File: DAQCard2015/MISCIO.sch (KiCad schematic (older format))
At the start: 34 parts, among them K1 1462042-8, P10 SPYPAD, P11 70246-1004, P3 miniDIL20, P4 LEMO_EPY.00.250.NTN, P5 LEMO_EPY.00.250.NTN, P6 FAN, P8 SPYPAD, P9 SHV, Q1 MMBT2222A-TP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

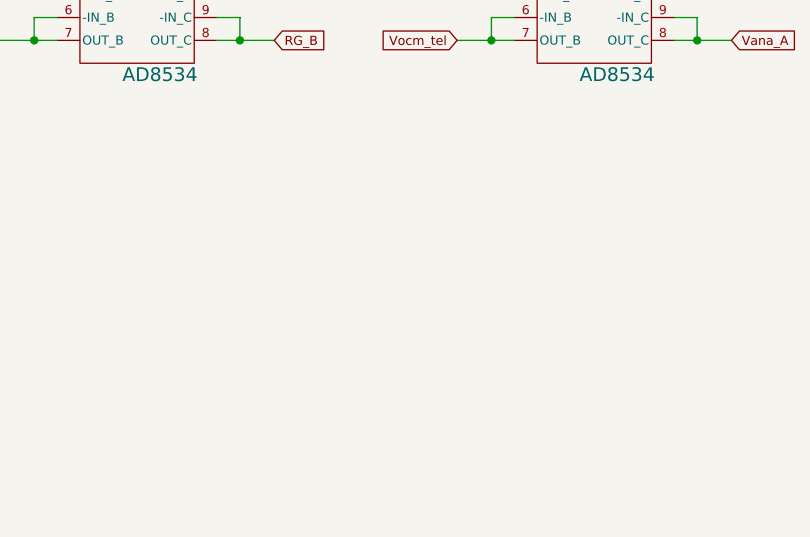
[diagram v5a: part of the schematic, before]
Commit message: Update V1.0 of DAQ Board Includes LED Driver for RJ45 Port, repositioning of JTAG
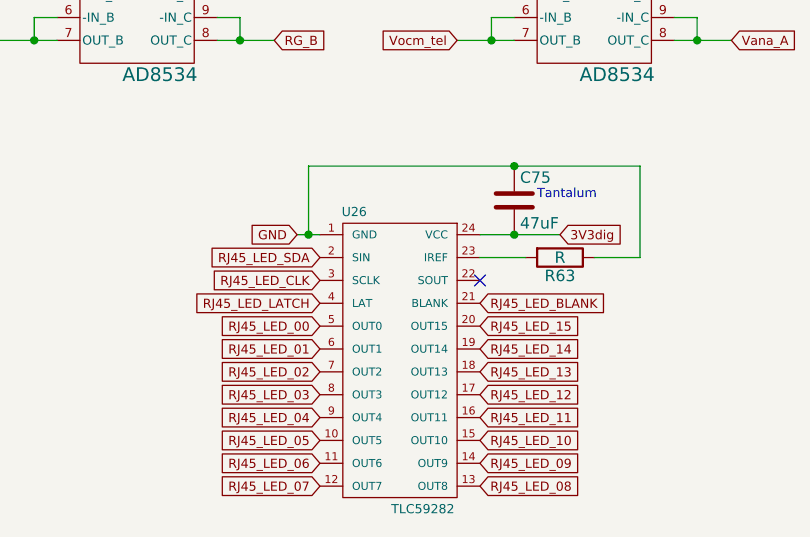
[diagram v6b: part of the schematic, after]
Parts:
- added C75: 47uF, Capacitors_Tantalum_SMD:TantalC_SizeD_EIA-7343_Reflow, symbol C
- added R63: R, Resistors_SMD:R_0603_HandSoldering, symbol R
- added U26: TLC59282, Housings_SSOP:SSOP-24_3.9x8.7mm_Pitch0.635mm, symbol TLC59282
- P10, P8: value SPYPAD -> GND
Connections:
- net 3V3dig: now also C75.2, U26.24 (VCC)
- net GND: now also C75.1, R63.1, U26.1 (GND)
- new net: R63.2, U26.23 (IREF)
- new net RJ45_LED_00: U26.5 (OUT0)
- new net RJ45_LED_01: U26.6 (OUT1)
- new net RJ45_LED_02: U26.7 (OUT2)
- new net RJ45_LED_03: U26.8 (OUT3)
- new net RJ45_LED_04: U26.9 (OUT4)
- new net RJ45_LED_05: U26.10 (OUT5)
- new net RJ45_LED_06: U26.11 (OUT6)
- new net RJ45_LED_07: U26.12 (OUT7)
- new net RJ45_LED_08: U26.13 (OUT8)
- new net RJ45_LED_09: U26.14 (OUT9)
- new net RJ45_LED_10: U26.15 (OUT10)
- new net RJ45_LED_11: U26.16 (OUT11)
- new net RJ45_LED_12: U26.17 (OUT12)
- new net RJ45_LED_13: U26.18 (OUT13)
- new net RJ45_LED_14: U26.19 (OUT14)
- new net RJ45_LED_15: U26.20 (OUT15)
- new net RJ45_LED_BLANK: U26.21 (BLANK)
- new net RJ45_LED_CLK: U26.3 (SCLK)
- new net RJ45_LED_LATCH: U26.4 (LAT)
- new net RJ45_LED_SDA: U26.2 (SIN)
- no-connect marks 4 -> 5
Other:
- note added: "Tantalum"
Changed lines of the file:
@@
 P 8250 5750
 F 0 "P8" H 8330 5750 40  0000 L CNN
-F 1 "SPYPAD" H 8250 5800 30  0001 C CNN
+F 1 "GND" H 8250 5800 30  0001 C CNN
 F 2 "extras:Harwin_D3082-05" H 8250 5750 60  0001 C CNN
 F 3 "" H 8250 5750 60  0000 C CNN
@@
 P 8400 5750
 F 0 "P10" H 8480 5750 40  0000 L CNN
-F 1 "SPYPAD" H 8400 5800 30  0001 C CNN
+F 1 "GND" H 8400 5800 30  0001 C CNN
 F 2 "extras:Harwin_D3082-05" H 8400 5750 60  0001 C CNN
 F 3 "" H 8400 5750 60  0000 C CNN
@@
 Wire Wire Line
 	1700 3350 2400 3350
+$Comp
+L TLC59282 U26
+U 1 1 560DFA19
+P 3100 6700
+F 0 "U26" H 2900 7350 40  0000 C CNN
+F 1 "TLC59282" H 3200 6050 40  0000 C CNN
+F 2 "Housings_SSOP:SSOP-24_3.9x8.7mm_Pitch0.635mm" H 3100 6700 40  0001 C CNN
+F 3 "" H 3100 6700 40  0000 C CNN
+	1    3100 6700
+	1    0    0    -1
+$EndComp
+Text GLabel 2650 6150 0    40   Input ~ 0
+GND
+Text GLabel 3800 6150 2    40   Input ~ 0
+3V3dig
+Wire Wire Line
+	3450 6150 3800 6150
+$Comp
+L C C75
+U 1 1 560DFC66
+P 3600 6000
+F 0 "C75" H 3625 6100 50  0000 L CNN
+F 1 "47uF" H 3625 5900 50  0000 L CNN
+F 2 "Capacitors_Tantalum_SMD:TantalC_SizeD_EIA-7343_Reflow" H 3638 5850 30  0001 C CNN
+F 3 "" H 3600 6000 60  0000 C CNN
+	1    3600 6000
+	1    0    0    -1
+$EndComp
+Connection ~ 3600 6150
+Wire Wire Line
+	2700 5850 4150 5850
+Wire Wire Line
+	2750 6150 2650 6150
+Wire Wire Line
+	2700 5850 2700 6150
+Connection ~ 2700 6150
+Text Notes 3700 6000 0    40   ~ 0
+Tantalum
+Text GLabel 2750 6250 0    40   Input ~ 0
+RJ45_LED_SDA
+Text GLabel 2750 6350 0    40   Input ~ 0
+RJ45_LED_CLK
+Text GLabel 2750 6450 0    40   Input ~ 0
+RJ45_LED_LATCH
+Text GLabel 3450 6450 2    40   Input ~ 0
+RJ45_LED_BLANK
+NoConn ~ 3450 6350
+$Comp
+L R R63
+U 1 1 560E0E6E
+P 3800 6250
+F 0 "R63" V 3880 6250 50  0000 C CNN
+F 1 "R" V 3800 6250 50  0000 C CNN
+F 2 "Resistors_SMD:R_0603_HandSoldering" V 3730 6250 30  0001 C CNN
+F 3 "" H 3800 6250 30  0000 C CNN
+	1    3800 6250
+	0    1    1    0
+$EndComp
+Wire Wire Line
+	3650 6250 3450 6250
+Wire Wire Line
+	3950 6250 4150 6250
+Wire Wire Line
+	4150 6250 4150 5850
+Connection ~ 3600 5850
+Text GLabel 2750 6550 0    40   Input ~ 0
+RJ45_LED_00
+Text GLabel 2750 6650 0    40   Input ~ 0
+RJ45_LED_01
+Text GLabel 2750 6750 0    40   Input ~ 0
+RJ45_LED_02
+Text GLabel 2750 6850 0    40   Input ~ 0
+RJ45_LED_03
+Text GLabel 2750 6950 0    40   Input ~ 0
+RJ45_LED_04
+Text GLabel 2750 7050 0    40   Input ~ 0
+RJ45_LED_05
+Text GLabel 2750 7150 0    40   Input ~ 0
+RJ45_LED_06
+Text GLabel 2750 7250 0    40   Input ~ 0
+RJ45_LED_07
+Text GLabel 3450 7250 2    40   Input ~ 0
+RJ45_LED_08
+Text GLabel 3450 7150 2    40   Input ~ 0
+RJ45_LED_09
+Text GLabel 3450 7050 2    40   Input ~ 0
+RJ45_LED_10
+Text GLabel 3450 6950 2    40   Input ~ 0
+RJ45_LED_11
+Text GLabel 3450 6850 2    40   Input ~ 0
+RJ45_LED_12
+Text GLabel 3450 6650 2    40   Input ~ 0
+RJ45_LED_14
+Text GLabel 3450 6750 2    40   Input ~ 0
+RJ45_LED_13
+Text GLabel 3450 6550 2    40   Input ~ 0
+RJ45_LED_15
 $EndSCHEMATC

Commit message: Adds digipart field to all parts that is now used in automatic generation of BOM(see DAQCard2015.html)
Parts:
- added C77, C79: 10uF, Capacitors_SMD:C_0805, symbol C
- added P18: Aref_A, extras:testpad, symbol SPYPAD
- added P19: Aref_B, extras:testpad, symbol SPYPAD
- added P20: RG_A, extras:testpad, symbol SPYPAD
- added P21: RG_B, extras:testpad, symbol SPYPAD
- added P22: Vthresh, extras:testpad, symbol SPYPAD
- added P23: Vocm, extras:testpad, symbol SPYPAD
- added P24: Vana_B, extras:testpad, symbol SPYPAD
- added P25: Vana_A, extras:testpad, symbol SPYPAD
- added P26: CASE GND, extras:TE_1217133-1, symbol SHV
- C70: digipart (none) -> 478-2991-1-ND
- C75: digipart (none) -> 478-9200-1-ND
- C76: digipart (none) -> 445-1316-1-ND
- D1: digipart (none) -> 350-3555-ND
- D2: digipart (none) -> SMAJ75ALFCT-ND
- K1: digipart (none) -> PB1249CT-ND
- P11: digipart (none) -> WM3478-ND
- P3: digipart (none) -> 952-1392-ND
- P4, P5: digipart (none) -> 1124-1358-ND
- P6: digipart (none) -> A1921-ND
- P9: value SHV -> HV; digipart (none) -> A100449CT-ND
- Q1, Q2: digipart (none) -> MMBT2222ATPMSCT-ND
- R50: value R -> 300R; digipart (none) -> P300HCT-ND
- R51, R52, R62: value R -> 30R; digipart (none) -> P30.0HCT-ND
- R53, R54: digipart (none) -> P10.0KHCT-ND
- R55: digipart (none) -> P49.9KFCT-ND
- R56: value 253R -> 249R; digipart (none) -> P249HCT-ND
- R57, R59: digipart (none) -> P470KECT-ND
- R58, R60: digipart (none) -> P51KECT-ND
- R61: digipart (none) -> P5.10KHCT-ND
- R63: value R -> 2k; digipart (none) -> P2.00KHCT-ND
- RV1: digipart (none) -> SM-31TW103CT-ND
- TH1: digipart (none) -> 445-2554-1-ND
- U19, U23: digipart (none) -> AD8534ARUZ-REELCT-ND
- U22: digipart (none) -> AD5628ARUZ-2-ND
- U24: digipart (none) -> MCP65R41T-2402E/CHYCT-ND
- U26: digipart (none) -> 296-28098-1-ND
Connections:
- net 5Vdig: now also C77.2, C79.2
- net Aref_A: now also P18.1
- net Aref_B: now also P19.1
- net GND: now also C77.1, C79.1, P26.1 (In)
- net RG_A: now also P20.1
- net RG_B: now also P21.1
- net Vana_A: now also P25.1
- net Vana_B: now also P24.1
- net Vocm_tel: now also P23.1
- net Vthresh: now also P22.1
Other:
- moved on the sheet: U23

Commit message: annotates parts for new build-management tool
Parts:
- C70: Digikey (none) -> 478-2991-1-ND; digipart 478-2991-1-ND -> (none)
- C75: Digikey (none) -> 478-9200-1-ND; digipart 478-9200-1-ND -> (none)
- C76: Digikey (none) -> 445-1316-1-ND; digipart 445-1316-1-ND -> (none)
- C77, C79: Digikey (none) -> 445-11464-1-ND; digipart 445-11464-1-ND -> (none)
- D1: Digikey (none) -> 350-3555-ND; digipart 350-3555-ND -> (none)
- D2: Digikey (none) -> SMAJ75ALFCT-ND; digipart SMAJ75ALFCT-ND -> (none)
- K1: Digikey (none) -> PB1249CT-ND; digipart PB1249CT-ND -> (none)
- P11: Digikey (none) -> WM3478-ND; digipart WM3478-ND -> (none)
- P26, P9: Digikey (none) -> A100449CT-ND; digipart A100449CT-ND -> (none)
- P3: Digikey (none) -> 952-1392-ND; digipart 952-1392-ND -> (none)
- P4, P5: Digikey (none) -> 1124-1358-ND; digipart 1124-1358-ND -> (none)
- P6: Digikey (none) -> A1921-ND; digipart A1921-ND -> (none)
- Q1, Q2: Digikey (none) -> MMBT2222ATPMSCT-ND; digipart MMBT2222ATPMSCT-ND -> (none)
- R50: Digikey (none) -> P300HCT-ND; digipart P300HCT-ND -> (none)
- R51, R52, R62: Digikey (none) -> P30.0HCT-ND; digipart P30.0HCT-ND -> (none)
- R53, R54: Digikey (none) -> P10.0KHCT-ND; digipart P10.0KHCT-ND -> (none)
- R55: Digikey (none) -> P49.9KFCT-ND; digipart P49.9KFCT-ND -> (none)
- R56: Digikey (none) -> P249HCT-ND; digipart P249HCT-ND -> (none)
- R57, R59: Digikey (none) -> P470KECT-ND; digipart P470KECT-ND -> (none)
- R58, R60: Digikey (none) -> P51KECT-ND; digipart P51KECT-ND -> (none)
- R61: Digikey (none) -> P5.10KHCT-ND; digipart P5.10KHCT-ND -> (none)
- R63: Digikey (none) -> P2.00KHCT-ND; digipart P2.00KHCT-ND -> (none)
- RV1: symbol POT -> POT-RESCUE-DAQCard2015; Digikey (none) -> SM-31TW103CT-ND; digipart SM-31TW103CT-ND -> (none)
- TH1: Digikey (none) -> 445-2554-1-ND; digipart 445-2554-1-ND -> (none)
- U19, U23: Digikey (none) -> AD8534ARUZ-REELCT-ND; digipart AD8534ARUZ-REELCT-ND -> (none)
- U22: Digikey (none) -> AD5628ARUZ-2-ND; digipart AD5628ARUZ-2-ND -> (none)
- U24: Digikey (none) -> MCP65R41T-2402E/CHYCT-ND; digipart MCP65R41T-2402E/CHYCT-ND -> (none)
- U26: Digikey (none) -> 296-28098-1-ND; digipart 296-28098-1-ND -> (none)
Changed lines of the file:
@@
 EESchema Schematic File Version 2
+LIBS:DAQCard2015-rescue
 LIBS:power
 LIBS:device
@@
 F 2 "extras:EPY.00.250.NTN" H 10650 1350 60  0001 C CNN
 F 3 "" H 10650 1350 60  0000 C CNN
-F 4 "1124-1358-ND" H 10650 1350 60  0001 C CNN "digipart"
+F 4 "1124-1358-ND" H 10650 1350 60  0001 C CNN "Digikey"
 	1    10650 1350
 	1    0    0    -1
@@
 F 2 "extras:EPY.00.250.NTN" H 10400 1950 60  0001 C CNN
 F 3 "" H 10400 1950 60  0000 C CNN
-F 4 "1124-1358-ND" H 10400 1950 60  0001 C CNN "digipart"
+F 4 "1124-1358-ND" H 10400 1950 60  0001 C CNN "Digikey"
 	1    10400 1950
 	1    0    0    -1
@@
 F 2 "extras:M50-3101045" H 9250 1800 60  0001 C CNN
 F 3 "" H 9250 1800 60  0000 C CNN
-F 4 "952-1392-ND" H 9250 1800 60  0001 C CNN "digipart"
+F 4 "952-1392-ND" H 9250 1800 60  0001 C CNN "Digikey"
 	1    9250 1800
 	1    0    0    -1
@@
 F 2 "Resistors_SMD:R_0603" V 8030 3750 30  0001 C CNN
 F 3 "" H 8100 3750 30  0000 C CNN
-F 4 "P10.0KHCT-ND" V 8100 3750 60  0001 C CNN "digipart"
+F 4 "P10.0KHCT-ND" V 8100 3750 60  0001 C CNN "Digikey"
 	1    8100 3750
 	1    0    0    -1
@@
 F 2 "Resistors_SMD:R_0603" V 8530 3750 30  0001 C CNN
 F 3 "" H 8600 3750 30  0000 C CNN
-F 4 "P10.0KHCT-ND" V 8600 3750 60  0001 C CNN "digipart"
+F 4 "P10.0KHCT-ND" V 8600 3750 60  0001 C CNN "Digikey"
 	1    8600 3750
 	1    0    0    -1
 $EndComp
 $Comp
-L POT RV1
+L POT-RESCUE-DAQCard2015 RV1
 U 1 1 55F0172C
 P 8100 4550
+AR Path="/55F0172C" Ref="RV1"  Part="1"
+AR Path="/55C9D43F/55F0172C" Ref="RV1"  Part="1"
 F 0 "RV1" H 8100 4450 50  0000 C CNN
 F 1 "10k" H 8100 4550 50  0000 C CNN
 F 2 "extras:SM31TW+0805" H 8100 4550 60  0001 C CNN
 F 3 "" H 8100 4550 60  0000 C CNN
-F 4 "SM-31TW103CT-ND" H 8100 4550 60  0001 C CNN "digipart"
+F 4 "SM-31TW103CT-ND" H 8100 4550 60  0001 C CNN "Digikey"
 	1    8100 4550
 	0    1    1    0
@@
 F 2 "Housings_SOT-23_SOT-143_TSOT-6:SOT-23-6" H 9100 4050 60  0001 C CNN
 F 3 "" H 9100 4050 60  0000 C CNN
-F 4 "MCP65R41T-2402E/CHYCT-ND" H 9100 4050 60  0001 C CNN "digipart"
+F 4 "MCP65R41T-2402E/CHYCT-ND" H 9100 4050 60  0001 C CNN "Digikey"
 	1    9100 4050
 	1    0    0    -1
@@
 F 2 "Resistors_SMD:R_0603" H 8600 4450 60  0001 C CNN
 F 3 "" H 8600 4450 60  0000 C CNN
-F 4 "445-2554-1-ND" V 8600 4450 60  0001 C CNN "digipart"
+F 4 "445-2554-1-ND" V 8600 4450 60  0001 C CNN "Digikey"
 	1    8600 4450
 	1    0    0    -1
@@
 F 2 "Resistors_SMD:R_0603" V 9680 4050 30  0001 C CNN
 F 3 "" H 9750 4050 30  0000 C CNN
-F 4 "P249HCT-ND" V 9750 4050 60  0001 C CNN "digipart"
+F 4 "P249HCT-ND" V 9750 4050 60  0001 C CNN "Digikey"
 	1    9750 4050
 	0    1    1    0
@@
 F 2 "Socket_Strips:Socket_Strip_Straight_1x02" H 10500 3650 60  0001 C CNN
 F 3 "" H 10500 3650 60  0000 C CNN
-F 4 "A1921-ND" H 10500 3650 60  0001 C CNN "digipart"
+F 4 "A1921-ND" H 10500 3650 60  0001 C CNN "Digikey"
 	1    10500 3650
 	1    0    0    -1
@@
 F 2 "Resistors_SMD:R_1206" V 8980 4350 30  0001 C CNN
 F 3 "" H 9050 4350 30  0000 C CNN
-F 4 "P49.9KFCT-ND" V 9050 4350 60  0001 C CNN "digipart"
+F 4 "P49.9KFCT-ND" V 9050 4350 60  0001 C CNN "Digikey"
 	1    9050 4350
 	0    1    1    0
@@
 F 2 "extras:1462042-8" H 3250 1050 60  0001 C CNN
 F 3 "" H 3250 1050 60  0000 C CNN
-F 4 "PB1249CT-ND" H 3250 1050 60  0001 C CNN "digipart"
+F 4 "PB1249CT-ND" H 3250 1050 60  0001 C CNN "Digikey"
 	1    3250 1050
 	1    0    0    -1
@@
 F 2 "Resistors_SMD:R_1206" V 2530 900 30  0001 C CNN
 F 3 "" H 2600 900 30  0000 C CNN
-F 4 "P470KECT-ND" V 2600 900 60  0001 C CNN "digipart"
+F 4 "P470KECT-ND" V 2600 900 60  0001 C CNN "Digikey"
 	1    2600 900
 	0    1    1    0
@@
 F 2 "Resistors_SMD:R_1206" V 2230 1250 30  0001 C CNN
 F 3 "" H 2300 1250 30  0000 C CNN
-F 4 "P470KECT-ND" V 2300 1250 60  0001 C CNN "digipart"
+F 4 "P470KECT-ND" V 2300 1250 60  0001 C CNN "Digikey"
 	1    2300 1250
 	0    1    1    0
@@
 F 2 "Capacitors_SMD:C_1812" H 1688 1300 30  0001 C CNN
 F 3 "" H 1650 1450 60  0000 C CNN
-F 4 "478-2991-1-ND" H 1650 1450 60  0001 C CNN "digipart"
+F 4 "478-2991-1-ND" H 1650 1450 60  0001 C CNN "Digikey"
 	1    1650 1450
 	1    0    0    -1
@@
 F 2 "Resistors_SMD:R_1206" V 2680 1650 30  0001 C CNN
 F 3 "" H 2750 1650 30  0000 C CNN
-F 4 "P51KECT-ND" V 2750 1650 60  0001 C CNN "digipart"
+F 4 "P51KECT-ND" V 2750 1650 60  0001 C CNN "Digikey"
 	1    2750 1650
 	0    1    1    0
@@
 F 2 "Resistors_SMD:R_1206" V 2280 1650 30  0001 C CNN
 F 3 "" H 2350 1650 30  0000 C CNN
-F 4 "P51KECT-ND" V 2350 1650 60  0001 C CNN "digipart"
+F 4 "P51KECT-ND" V 2350 1650 60  0001 C CNN "Digikey"
 	1    2350 1650
 	0    1    1    0
@@
 F 2 "Diodes_SMD:SMA_Standard" V 4000 1350 60  0001 C CNN
 F 3 "" V 4000 1350 60  0000 C CNN
-F 4 "SMAJ75ALFCT-ND" H 4000 1350 60  0001 C CNN "digipart"
+F 4 "SMAJ75ALFCT-ND" H 4000 1350 60  0001 C CNN "Digikey"
 	1    4000 1350
 	0    1    1    0
@@
 F 2 "Resistors_SMD:R_0603" V 4430 1800 30  0001 C CNN
 F 3 "" H 4500 1800 30  0000 C CNN
-F 4 "P5.10KHCT-ND" V 4500 1800 60  0001 C CNN "digipart"
+F 4 "P5.10KHCT-ND" V 4500 1800 60  0001 C CNN "Digikey"
 	1    4500 1800
 	0    1    1    0
@@
 F 2 "extras:TE_1217133-1" H 1850 1000 60  0001 C CNN
 F 3 "" H 1850 1000 60  0000 C CNN
-F 4 "A100449CT-ND" H 1850 1000 60  0001 C CNN "digipart"
+F 4 "A100449CT-ND" H 1850 1000 60  0001 C CNN "Digikey"
 	1    1850 1000
 	-1   0    0    1
@@
 F 2 "extras:Dialight_5690101372F" H 6350 1800 60  0001 C CNN
 F 3 "" H 6350 1800 60  0000 C CNN
-F 4 "350-3555-ND" V 6350 1800 60  0001 C CNN "digipart"
+F 4 "350-3555-ND" V 6350 1800 60  0001 C CNN "Digikey"
 	1    6350 1800
 	1    0    0    -1
@@
 F 2 "Resistors_SMD:R_0603" V 6280 1300 30  0001 C CNN
 F 3 "" H 6350 1300 30  0000 C CNN
-F 4 "P300HCT-ND" V 6350 1300 60  0001 C CNN "digipart"
+F 4 "P300HCT-ND" V 6350 1300 60  0001 C CNN "Digikey"
 	1    6350 1300
 	1    0    0    -1
@@
 F 2 "Resistors_SMD:R_0603" V 6580 1300 30  0001 C CNN
 F 3 "" H 6650 1300 30  0000 C CNN
-F 4 "P30.0HCT-ND" V 6650 1300 60  0001 C CNN "digipart"
+F 4 "P30.0HCT-ND" V 6650 1300 60  0001 C CNN "Digikey"
 	1    6650 1300
 	1    0    0    -1
@@
 F 2 "Resistors_SMD:R_0603" V 6880 1300 30  0001 C CNN
 F 3 "" H 6950 1300 30  0000 C CNN
-F 4 "P30.0HCT-ND" V 6950 1300 60  0001 C CNN "digipart"
+F 4 "P30.0HCT-ND" V 6950 1300 60  0001 C CNN "Digikey"
 	1    6950 1300
 	1    0    0    -1
@@
 F 2 "Resistors_SMD:R_0603" V 7180 1300 30  0001 C CNN
 F 3 "" H 7250 1300 30  0000 C CNN
-F 4 "P30.0HCT-ND" V 7250 1300 60  0001 C CNN "digipart"
+F 4 "P30.0HCT-ND" V 7250 1300 60  0001 C CNN "Digikey"
 	1    7250 1300
 	1    0    0    -1
@@
 F 2 "Housings_SOT-23_SOT-143_TSOT-6:SOT-23" H 10400 4150 29  0001 C CNN
 F 3 "" H 10200 4050 60  0000 C CNN
-F 4 "MMBT2222ATPMSCT-ND" H 10200 4050 60  0001 C CNN "digipart"
+F 4 "MMBT2222ATPMSCT-ND" H 10200 4050 60  0001 C CNN "Digikey"
 	1    10200 4050
 	1    0    0    -1
@@
 F 2 "extras:TSSOP-16_4.4x5mm_Pitch0.65mm" H 3150 3650 60  0001 C CNN
 F 3 "" H 3150 3650 60  0000 C CNN
-F 4 "AD5628ARUZ-2-ND" H 2950 3500 60  0001 C CNN "digipart"
+F 4 "AD5628ARUZ-2-ND" H 2950 3500 60  0001 C CNN "Digikey"
 	1    2950 3500
 	1    0    0    -1
@@
 F 2 "Housings_SSOP:TSSOP-14_4.4x5mm_Pitch0.65mm" H 1850 5150 60  0001 C CNN
 F 3 "" H 1850 5150 60  0000 C CNN
-F 4 "AD8534ARUZ-REELCT-ND" H 1950 5000 60  0001 C CNN "digipart"
+F 4 "AD8534ARUZ-REELCT-ND" H 1950 5000 60  0001 C CNN "Digikey"
 	1    1950 5000
 	1    0    0    -1
@@
 F 2 "Housings_SSOP:TSSOP-14_4.4x5mm_Pitch0.65mm" H 3950 5150 60  0001 C CNN
 F 3 "" H 3950 5150 60  0000 C CNN
-F 4 "AD8534ARUZ-REELCT-ND" H 4050 5000 60  0001 C CNN "digipart"
+F 4 "AD8534ARUZ-REELCT-ND" H 4050 5000 60  0001 C CNN "Digikey"
 	1    4050 5000
 	1    0    0    -1
@@
 F 2 "Housings_SOT-23_SOT-143_TSOT-6:SOT-23" H 4300 1900 29  0001 C CNN
 F 3 "" H 4100 1800 60  0000 C CNN
-F 4 "MMBT2222ATPMSCT-ND" H 4100 1800 60  0001 C CNN "digipart"
+F 4 "MMBT2222ATPMSCT-ND" H 4100 1800 60  0001 C CNN "Digikey"
 	1    4100 1800
 	-1   0    0    -1
@@
 F 2 "Capacitors_SMD:C_0603" H 1888 2950 30  0001 C CNN
 F 3 "" H 1850 3100 60  0000 C CNN
-F 4 "445-1316-1-ND" H 1850 3100 60  0001 C CNN "digipart"
+F 4 "445-1316-1-ND" H 1850 3100 60  0001 C CNN "Digikey"
 	1    1850 3100
 	1    0    0    -1
@@
 F 2 "Pin_Headers:Pin_Header_Straight_2x05" H 6450 1950 60  0001 C CNN
 F 3 "" H 6450 1950 60  0000 C CNN
-F 4 "WM3478-ND" H 6450 3150 60  0001 C CNN "digipart"
+F 4 "WM3478-ND" H 6450 3150 60  0001 C CNN "Digikey"
 	1    6450 3150
 	1    0    0    -1
@@
 F 2 "Housings_SSOP:SSOP-24_3.9x8.7mm_Pitch0.635mm" H 3100 6700 40  0001 C CNN
 F 3 "" H 3100 6700 40  0000 C CNN
-F 4 "296-28098-1-ND" H 3100 6700 60  0001 C CNN "digipart"
+F 4 "296-28098-1-ND" H 3100 6700 60  0001 C CNN "Digikey"
 	1    3100 6700
 	1    0    0    -1
@@
 F 2 "Capacitors_Tantalum_SMD:TantalC_SizeD_EIA-7343_Reflow" H 3638 5850 30  0001 C CNN
 F 3 "" H 3600 6000 60  0000 C CNN
-F 4 "478-9200-1-ND" H 3600 6000 60  0001 C CNN "digipart"
+F 4 "478-9200-1-ND" H 3600 6000 60  0001 C CNN "Digikey"
 	1    3600 6000
 	1    0    0    -1
@@
 F 2 "Resistors_SMD:R_0603_HandSoldering" V 3730 6250 30  0001 C CNN
 F 3 "" H 3800 6250 30  0000 C CNN
-F 4 "P2.00KHCT-ND" V 3800 6250 60  0001 C CNN "digipart"
+F 4 "P2.00KHCT-ND" V 3800 6250 60  0001 C CNN "Digikey"
 	1    3800 6250
 	0    1    1    0
@@
 F 2 "Capacitors_SMD:C_0805" H 3088 5050 30  0001 C CNN
 F 3 "" H 3050 5200 60  0000 C CNN
-F 4 "445-11464-1-ND" H 3050 5200 60  0001 C CNN "digipart"
+F 4 "445-11464-1-ND" H 3050 5200 60  0001 C CNN "Digikey"
 	1    3050 5200
 	-1   0    0    1
@@
 F 2 "Capacitors_SMD:C_0805" H 1038 5050 30  0001 C CNN
 F 3 "" H 1000 5200 60  0000 C CNN
-F 4 "445-11464-1-ND" H 1000 5200 60  0001 C CNN "digipart"
+F 4 "445-11464-1-ND" H 1000 5200 60  0001 C CNN "Digikey"
 	1    1000 5200
 	-1   0    0    1
@@
 F 2 "extras:TE_1217133-1" H 1500 750 60  0001 C CNN
 F 3 "" H 1500 750 60  0000 C CNN
-F 4 "A100449CT-ND" H 1500 750 60  0001 C CNN "digipart"
+F 4 "A100449CT-ND" H 1500 750 60  0001 C CNN "Digikey"
 	1    1500 750
 	0    -1   -1   0
